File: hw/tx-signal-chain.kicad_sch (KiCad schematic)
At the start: 8 parts, among them Q401 IRFP250NPBF, U401 UCC27511ADBV

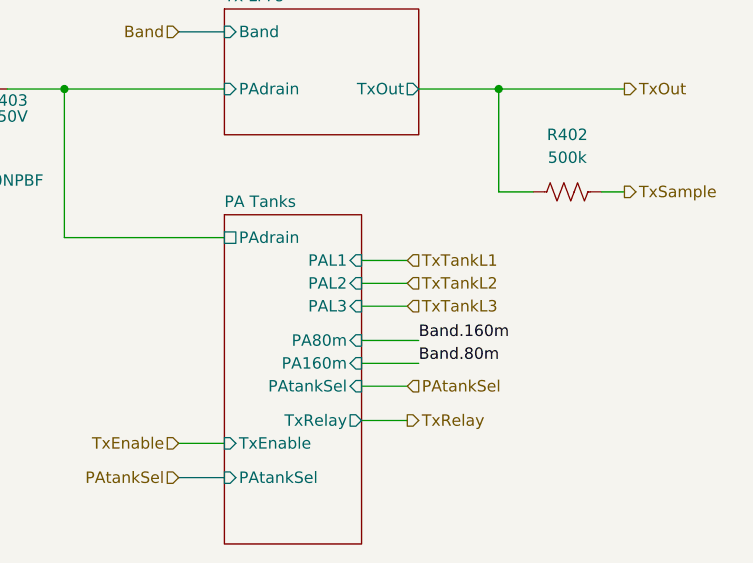
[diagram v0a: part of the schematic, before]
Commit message: Embarking on a whole new arch for rx without BPFs and using a single digitally tuned tank plus three QSDs to accomplish image rejection in digital domain
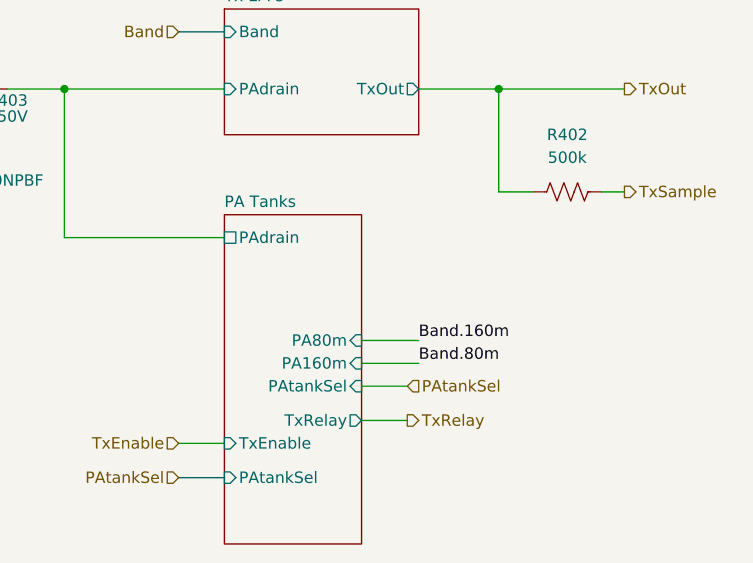
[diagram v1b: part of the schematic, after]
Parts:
- C401, C402, C403: footprint (none) -> Capacitor_SMD:C_0805_2012Metric
- Q401: footprint TO545P530X1560X2460-3P -> (none)
- R401: footprint (none) -> Resistor_SMD:R_1206_3216Metric
- R402: footprint (none) -> Resistor_SMD:R_0603_1608Metric
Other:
- sheet PA Tanks ports: added none; removed PAL1, PAL2, PAL3

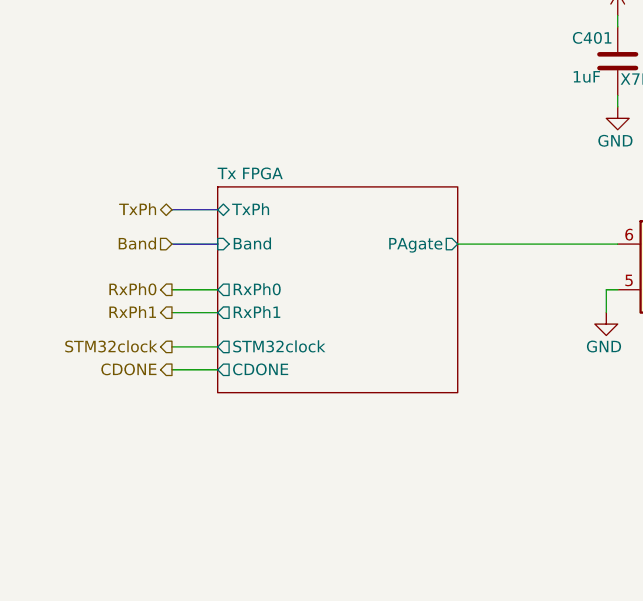
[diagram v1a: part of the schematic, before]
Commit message: Starting to switch to new rx architecture
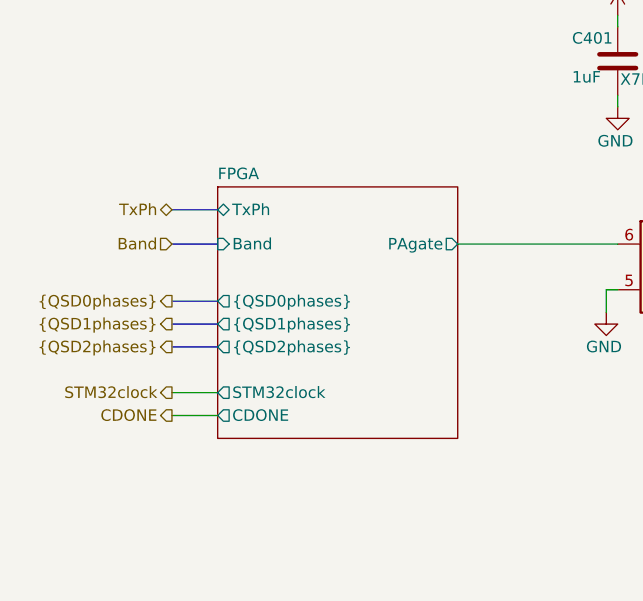
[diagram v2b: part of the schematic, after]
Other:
- sheet Tx FPGA renamed FPGA
- sheet FPGA ports: added {QSD0phases}, {QSD1phases}, {QSD2phases}; removed RxPh0, RxPh1
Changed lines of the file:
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@@
-	(wire
-		(pts
-			(xy 60.96 92.71) (xy 66.04 92.71)
-		)
-		(stroke
-			(width 0)
-			(type default)
-		)
-	)
 	(wire
 		(pts
@@
 		)
 	)
+	(bus
+		(pts
+			(xy 60.96 96.52) (xy 66.04 96.52)
+		)
+		(stroke
+			(width 0)
+			(type default)
+		)
+	)
+	(bus
+		(pts
+			(xy 60.96 93.98) (xy 66.04 93.98)
+		)
+		(stroke
+			(width 0)
+			(type default)
+		)
+	)
 	(wire
 		(pts
@@
 	(wire
 		(pts
-			(xy 60.96 99.06) (xy 66.04 99.06)
+			(xy 60.96 104.14) (xy 66.04 104.14)
 		)
 		(stroke
@@
 	(wire
 		(pts
-			(xy 60.96 96.52) (xy 66.04 96.52)
+			(xy 60.96 101.6) (xy 66.04 101.6)
 		)
 		(stroke
@@
 		)
 	)
+	(bus
+		(pts
+			(xy 60.96 91.44) (xy 66.04 91.44)
+		)
+		(stroke
+			(width 0)
+			(type default)
+		)
+	)
 	(wire
 		(pts
@@
 		(pts
 			(xy 190.5 67.31) (xy 195.58 67.31)
-		)
-		(stroke
-			(width 0)
-			(type default)
-		)
-	)
-	(wire
-		(pts
-			(xy 60.96 90.17) (xy 66.04 90.17)
 		)
 		(stroke
@@
 			)
 			(justify left bottom)
+		)
+	)
+	(hierarchical_label "{QSD2phases}"
+		(shape output)
+		(at 60.96 96.52 180)
+		(effects
+			(font
+				(size 1.27 1.27)
+			)
+			(justify right)
 		)
 	)
@@
 		)
 	)
+	(hierarchical_label "{QSD1phases}"
+		(shape output)
+		(at 60.96 93.98 180)
+		(effects
+			(font
+				(size 1.27 1.27)
+			)
+			(justify right)
+		)
+	)
 	(hierarchical_label "PAtankSel"
 		(shape input)
@@
 		)
 	)
-	(hierarchical_label "STM32clock"
+	(hierarchical_label "{QSD0phases}"
 		(shape output)
-		(at 60.96 96.52 180)
+		(at 60.96 91.44 180)
 		(effects
 			(font
@@
 		)
 	)
-	(hierarchical_label "RxPh1"
+	(hierarchical_label "STM32clock"
 		(shape output)
-		(at 60.96 92.71 180)
+		(at 60.96 101.6 180)
 		(effects
 			(font
@@
 		)
 	)
-	(hierarchical_label "RxPh0"
-		(shape output)
-		(at 60.96 90.17 180)
-		(effects
-			(font
-				(size 1.27 1.27)
-			)
-			(justify right)
-		)
-	)
 	(hierarchical_label "Band"
 		(shape input)
@@
 	(hierarchical_label "CDONE"
 		(shape output)
-		(at 60.96 99.06 180)
+		(at 60.96 104.14 180)
 		(effects
 			(font
@@
 	(sheet
 		(at 66.04 78.74)
-		(size 26.67 22.86)
+		(size 26.67 27.94)
 		(exclude_from_sim no)
 		(in_bom yes)
@@
 			(color 0 0 0 0.0000)
 		)
-		(property "Sheetname" "Tx FPGA"
+		(property "Sheetname" "FPGA"
 			(at 66.04 78.0284 0)
 			(effects
@@
 		)
 		(property "Sheetfile" "tx-fpga.kicad_sch"
-			(at 66.04 102.1846 0)
+			(at 66.04 107.2646 0)
 			(effects
 				(font
@@
 			)
 		)
-		(pin "RxPh0" output
-			(at 66.04 90.17 180)
+		(pin "STM32clock" output
+			(at 66.04 101.6 180)
 			(effects
 				(font
@@
 			)
 		)
-		(pin "RxPh1" output
-			(at 66.04 92.71 180)
+		(pin "CDONE" output
+			(at 66.04 104.14 180)
 			(effects
 				(font
@@
 			)
 		)
-		(pin "STM32clock" output
+		(pin "{QSD0phases}" output
+			(at 66.04 91.44 180)
+			(effects
+				(font
+					(size 1.27 1.27)
+				)
+				(justify left)
+			)
+		)
+		(pin "{QSD1phases}" output
+			(at 66.04 93.98 180)
+			(effects
+				(font
+					(size 1.27 1.27)
+				)
+				(justify left)
+			)
+		)
+		(pin "{QSD2phases}" output
 			(at 66.04 96.52 180)
 			(effects
 				(font
-					(size 1.27 1.27)
-				)
-				(justify left)
-			)
-		)
-		(pin "CDONE" output
-			(at 66.04 99.06 180)
-			(effects
-				(font

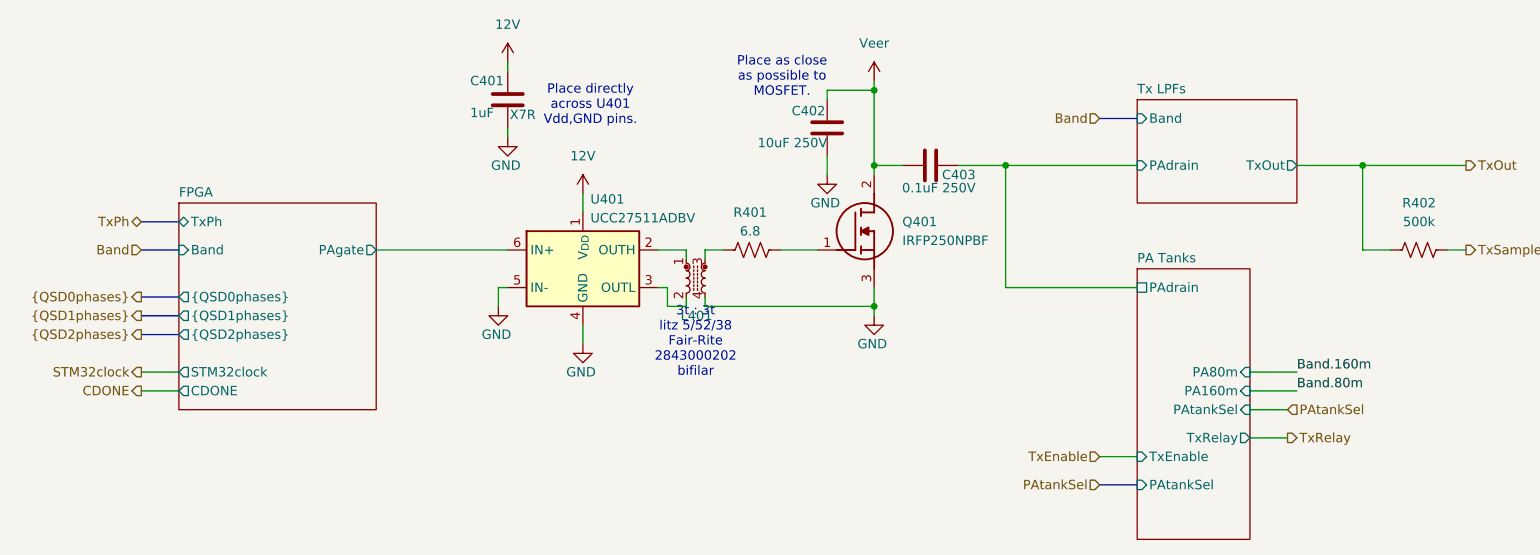
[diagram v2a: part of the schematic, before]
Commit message: Converting to use busses as global symbols instead of tedium. Using 2n7002 Nexperia dual MOSFET because of its LOW LOW capacitance spec for L, C, and attenuator switching.
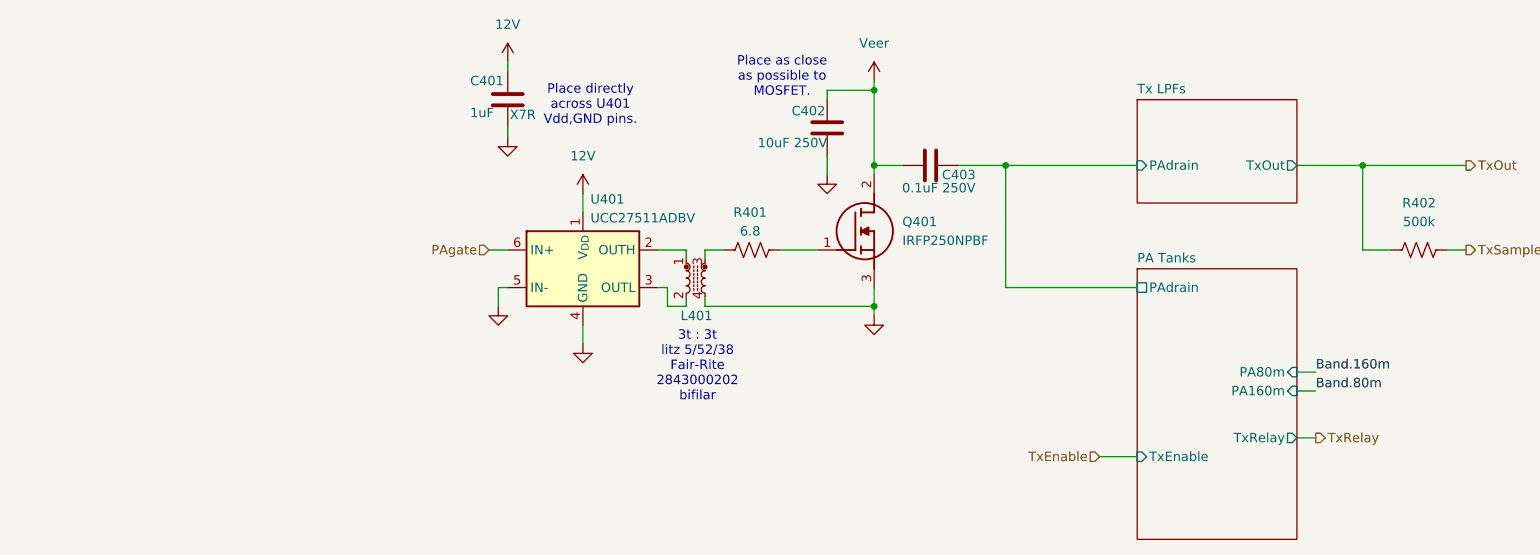
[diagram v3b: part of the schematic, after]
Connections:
- net FPGA/PAgate renamed PAgate
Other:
- removed sheet FPGA
- sheet PA Tanks ports: added none; removed PAtankSel
- sheet Tx LPFs ports: added none; removed Band

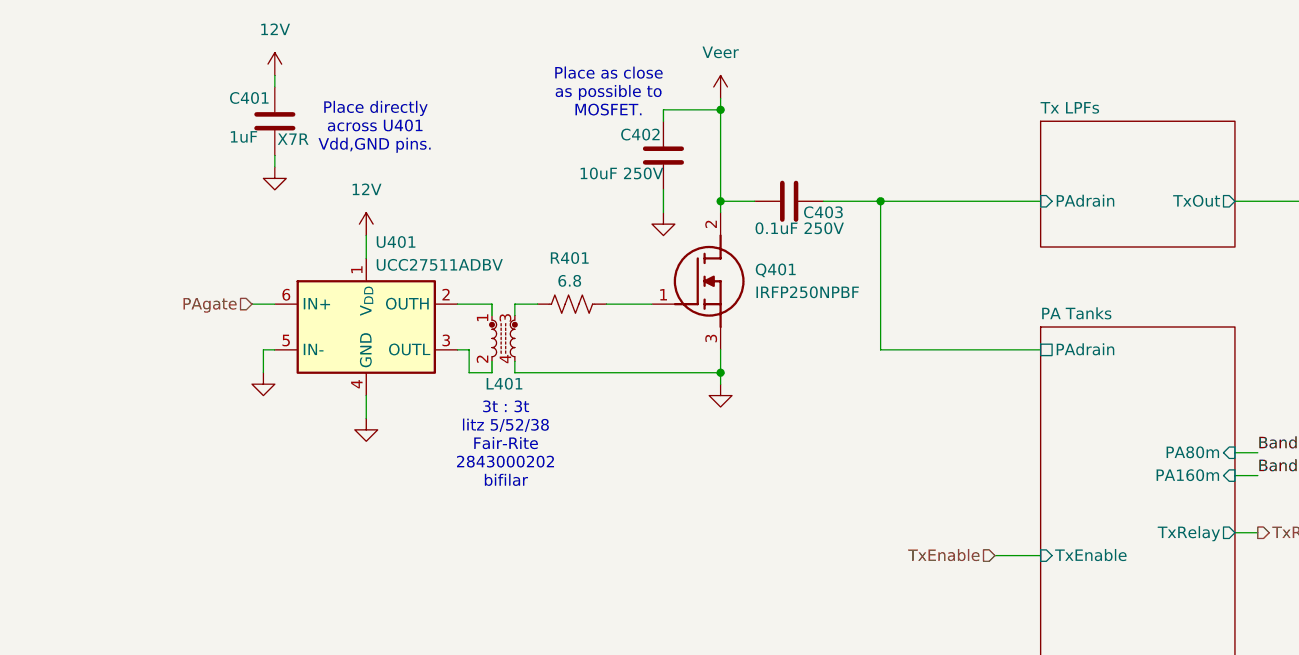
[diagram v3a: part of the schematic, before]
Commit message: More Tx LPF design and a doc. The schematic now reflects 200 ohm domain for the LPFs and the PA LC tanks too.
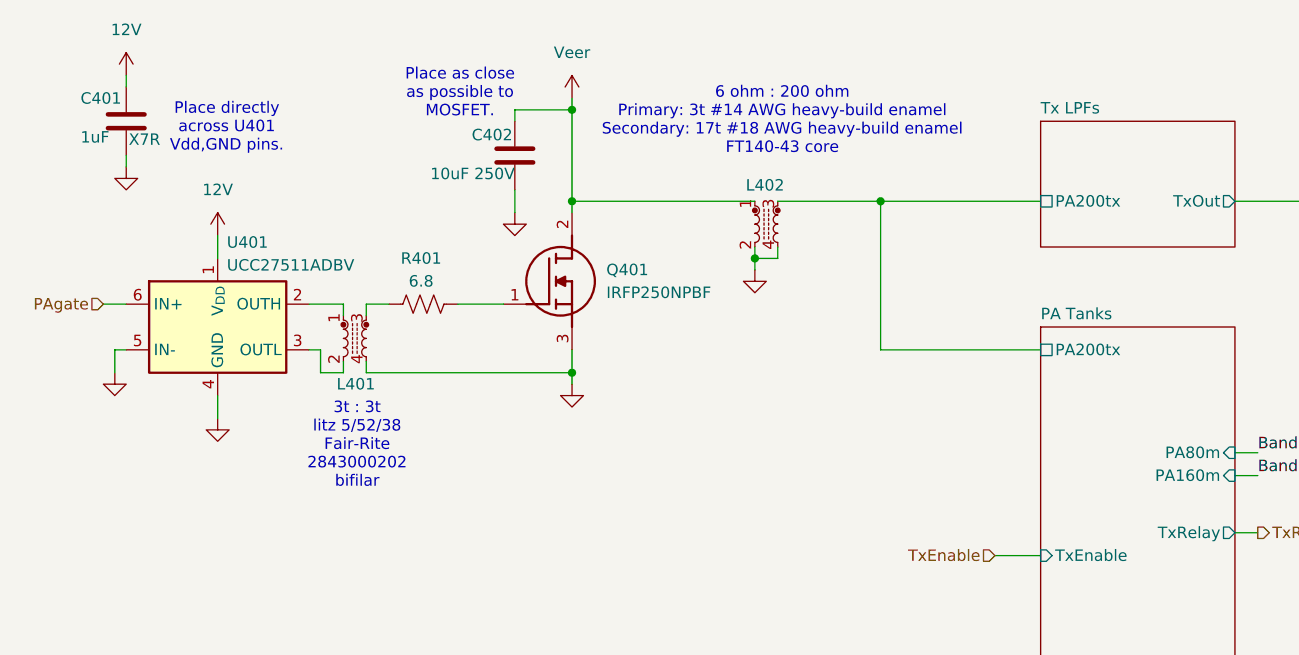
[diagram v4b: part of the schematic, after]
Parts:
- removed C403: 0.1uF 250V, Capacitor_SMD:C_0805_2012Metric, symbol Device:C
- added L402: ~, symbol Device:L_Ferrite_Coupled_Small
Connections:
- net GND: now also L402.2, L402.4
- net Veer: now also L402.1
- new net PA Tanks/PA200tx: L402.3
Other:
- sheet PA Tanks ports: added PA200tx; removed PAdrain
- sheet Tx LPFs ports: added PA200tx; removed PAdrain
- note added: "6 ohm : 200 ohm Primary: 3t #14 AWG heavy-build enamel Secondary: 17t #18 AWG heavy-build enamel FT140-43 core"
- moved on the sheet: C401, C402, L401, Q401, R401, U401

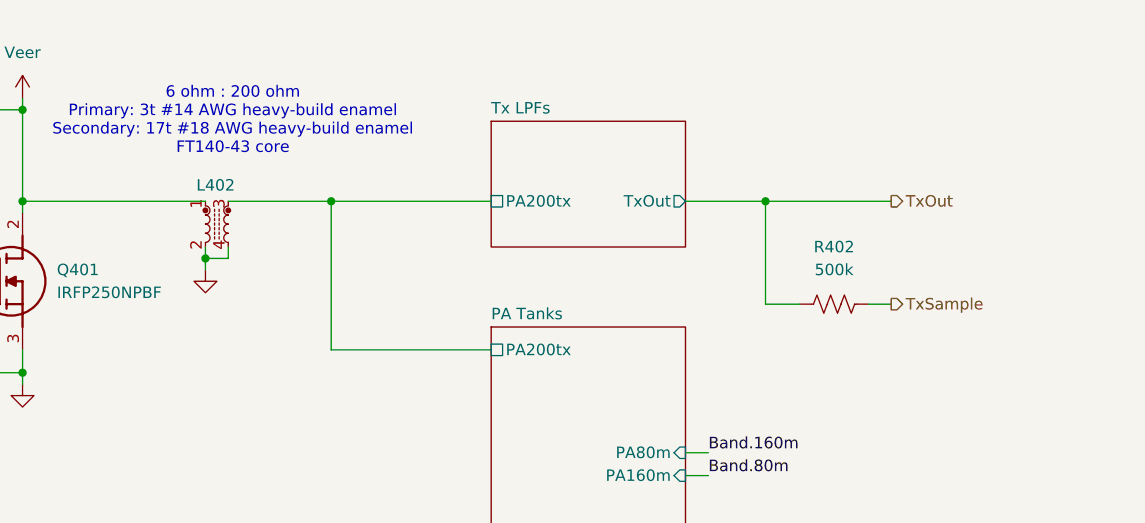
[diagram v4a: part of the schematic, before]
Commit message: Add more about balun for 200 -> 50 ohm - not done yet but started
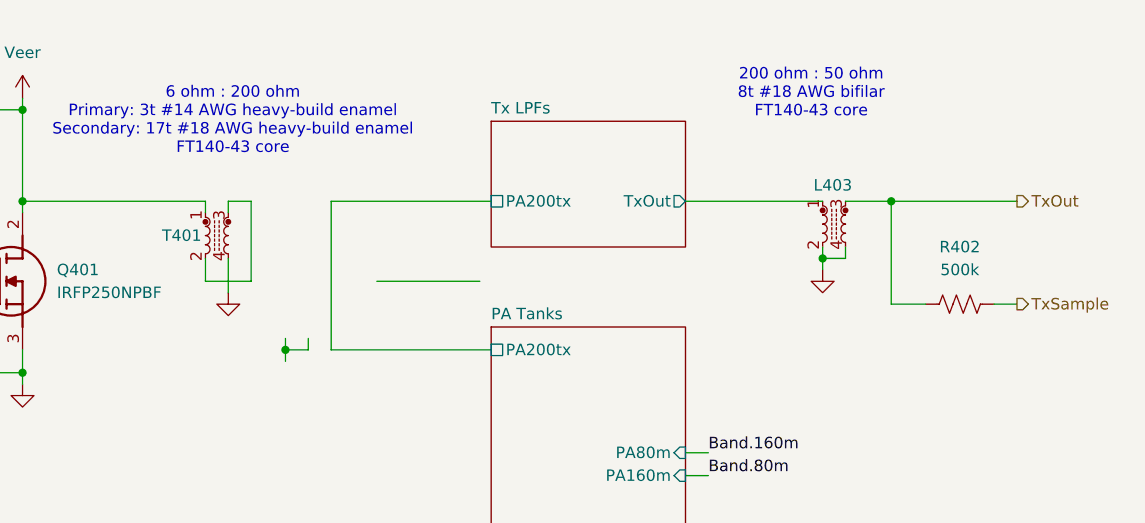
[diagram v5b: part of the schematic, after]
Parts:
- added L403: ~, symbol Device:L_Ferrite_Coupled_Small
- renumbered L402 to T401
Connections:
- net GND: now also L403.2, L403.4; no longer T401.2
- net PA Tanks/PA200tx: no longer T401.3
- net TxOut: now also L403.3
- new net: T401.2, T401.3
- new net Tx LPFs/TxOut: L403.1
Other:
- note added: "200 ohm : 50 ohm 8t #18 AWG bifilar FT140-43 core"
- moved on the sheet: R402, T401
